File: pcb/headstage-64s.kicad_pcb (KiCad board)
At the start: 6 copper layers, 19 x 19 mm, 119 parts, among them J1 Conn_Coaxial, J2 DF40C-70DP-0.4V(51), J5 PINHD-1x7_ONIXJTAG-RevA, SW1 R-668049, U1 RHD2164, U10 NCP163AFCT120T2G, U11 W25Q80EWUXIE, U12 DSC6011JI1A-050.0000, U13 NCP163AFCT330T2G, U2 TS4231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

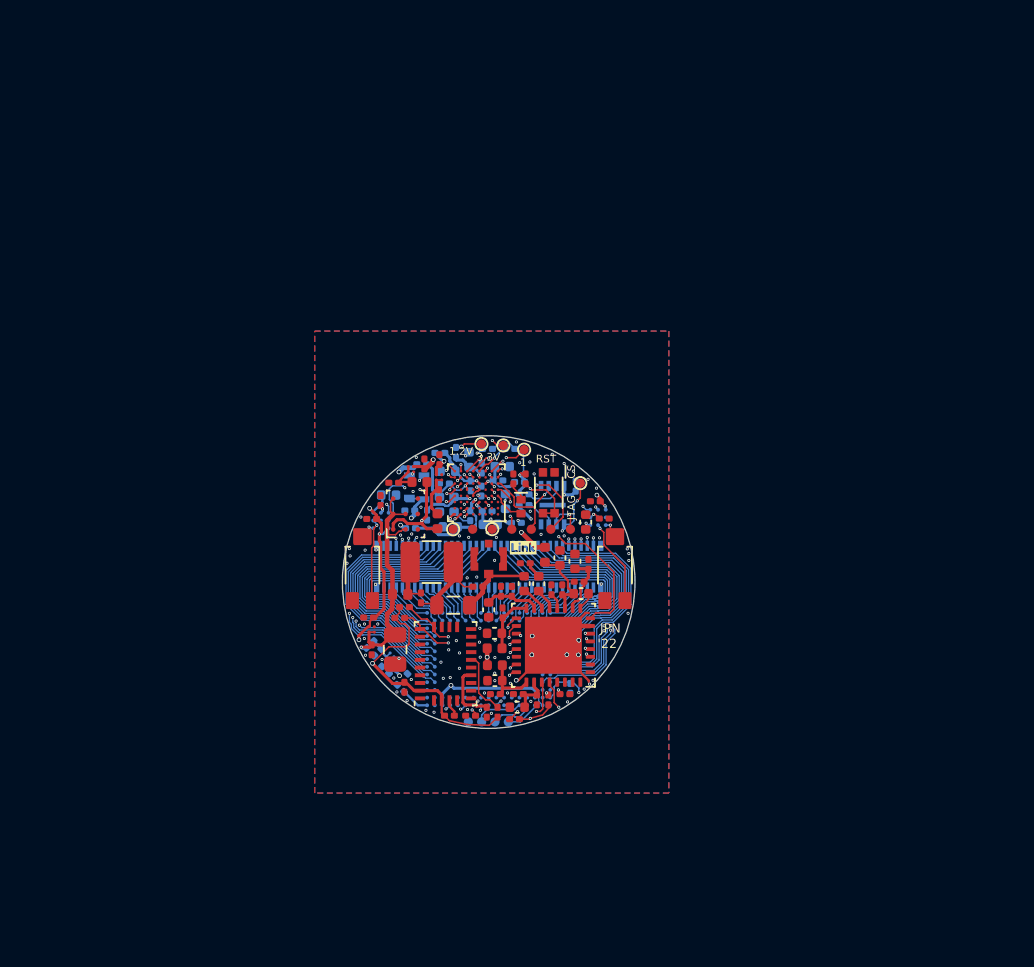
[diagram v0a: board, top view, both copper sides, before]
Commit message: Rev. A initial design prior to fab comments
- BOM simplification
- Added my initials to the board
- Made the board more easy to panlize
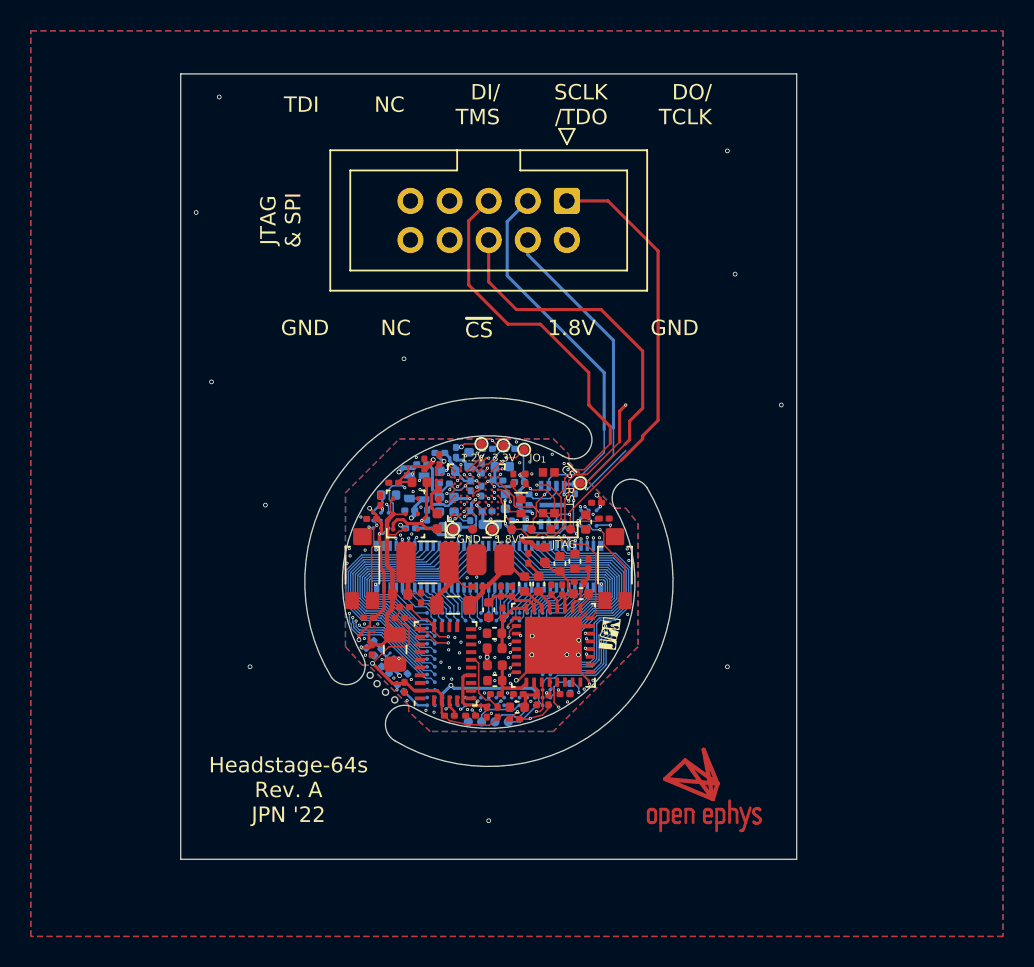
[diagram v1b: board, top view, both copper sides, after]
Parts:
- removed kibuzzard-61E6E0C5: G***, kibuzzard-61E6E0C5
- added ?: , jonnew-eagle:OE-LOGO-7X5, F.Cu at (137.2, 77.3)
- added G***: LOGO, LOGO, F.Cu at (131.3, 66.3)
- added J3: SBH11-PBPC-D05-ST-BK, Connector_IDC:IDC-Header_2x05_P2.54mm_Vertical, F.Cu at (128.6, 38.2)
- added JP1: Jumper_2_Open, jonnew:OE_SolderJumper-2_0201_Open_Pad, B.Cu at (125.9, 59.2)
- C51, C52: value 1.0uF -> 1uF
- D2: value LED -> SML-P11UTT86R
- J1: value Conn_Coaxial -> CONMHF4-SMD-G-T; footprint jonnew:LINX_CONMHF4-SMD-G -> Headstage-64s:Coax-Adapter
- R3: value ? -> 39.2,1%
- R4: value ? -> 78.7k,1%
- R6: value ? -> 40.2k,1%
- U5: value TPS8269xxxSIPR -> TPS82695
- moved U6 0.60 mm to (130.0, 58.9)
- moved REF** 0.44 mm to (126.6, 55.2)
- moved R15 0.38 mm to (126.1, 61.5), turned to 90 degrees
- moved C35 0.38 mm to (128.1, 61.8)
- moved L12 0.36 mm to (125.0, 59.4), turned to 90 degrees
- moved L3 0.27 mm to (119.5, 61.7)
- moved C42 0.18 mm to (129.1, 57.0), turned to -90 degrees
- moved C26 0.12 mm to (130.5, 57.9)
- moved J1 0.12 mm to (123.6, 61.5)
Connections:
- U11 pad 1: /FPGA/~{CS}_{Flash} -> Net-(JP1-Pad1)
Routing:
- net /FPGA/TDI: track 3.01 -> 42.6 mm, vias 2 -> 3
- net /FPGA/DO_{Flash}/TCK: track 7.82 -> 34.5 mm
- net /FPGA/DI_{Flash}/TMS: track 7.74 -> 34.1 mm
- net /FPGA/~{CS}_{Flash}: track 9.74 -> 35.7 mm, vias 3 -> 4
- net /FPGA/SCLK_{Flash}/TDO: track 6.64 -> 30.9 mm
- net +1V8: track 49.6 -> 68.5 mm
- net GND: track 14.2 -> 17.6 mm, vias 89 -> 101
- net Net-(JP1-Pad1): track 0.00 -> 3.02 mm
- net /FPGA/PDB_{Ser}: track 19.4 -> 17.7 mm
- net /DC Tap & Regulation/RF+DC: track 4.98 -> 6.04 mm
- net Net-(R17-Pad2): track 0.78 -> 1.72 mm
- net /3D Pose/PD_{1}-: track 1.17 -> 1.79 mm
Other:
- board size 19 x 19 mm -> 40 x 51 mm
- board text added: "1.8V"
- board text added: "DI/ TMS"
- board text added: "DO/ TCLK"
- board text added: "Headstage-64s Rev. A JPN '22"
- board text added: "IO_{1}"
- board text added: "JTAG & SPI"
- board text added: "NC"
- board text added: "SCLK /TDO"
- board text added: "TDI"
- board text removed: "'22"
- board text removed: "1"
- board text removed: "JPN"

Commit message: Small changes before speedy fabrication
- This is revision A
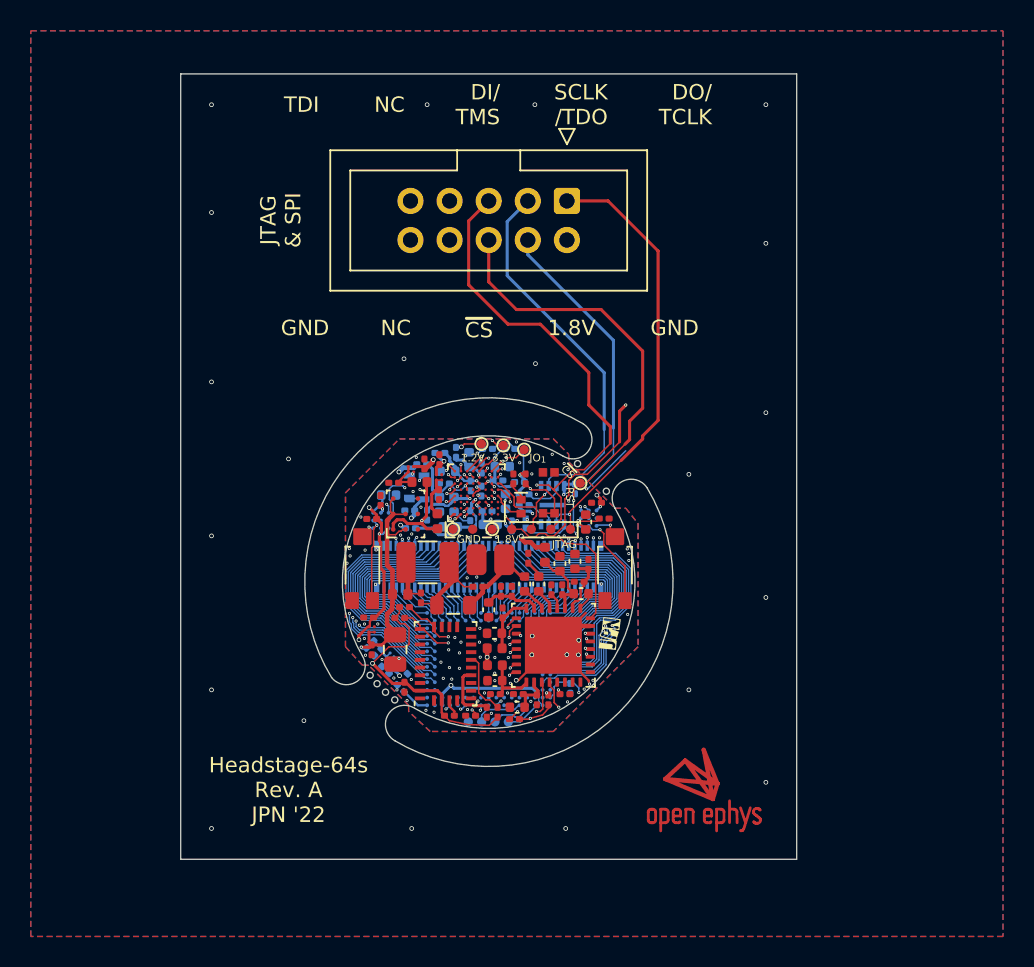
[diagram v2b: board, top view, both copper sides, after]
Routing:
- net GND: vias 101 -> 111
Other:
- outline, holes or cut-outs redrawn

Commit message: Start of revision B
- Address the following issues
1. The photodiode anode is on pin 3, not pin 2
2. No paste on coax connector
3. CRESET_B needs to come out to programming header
4. Need PU on CS line.
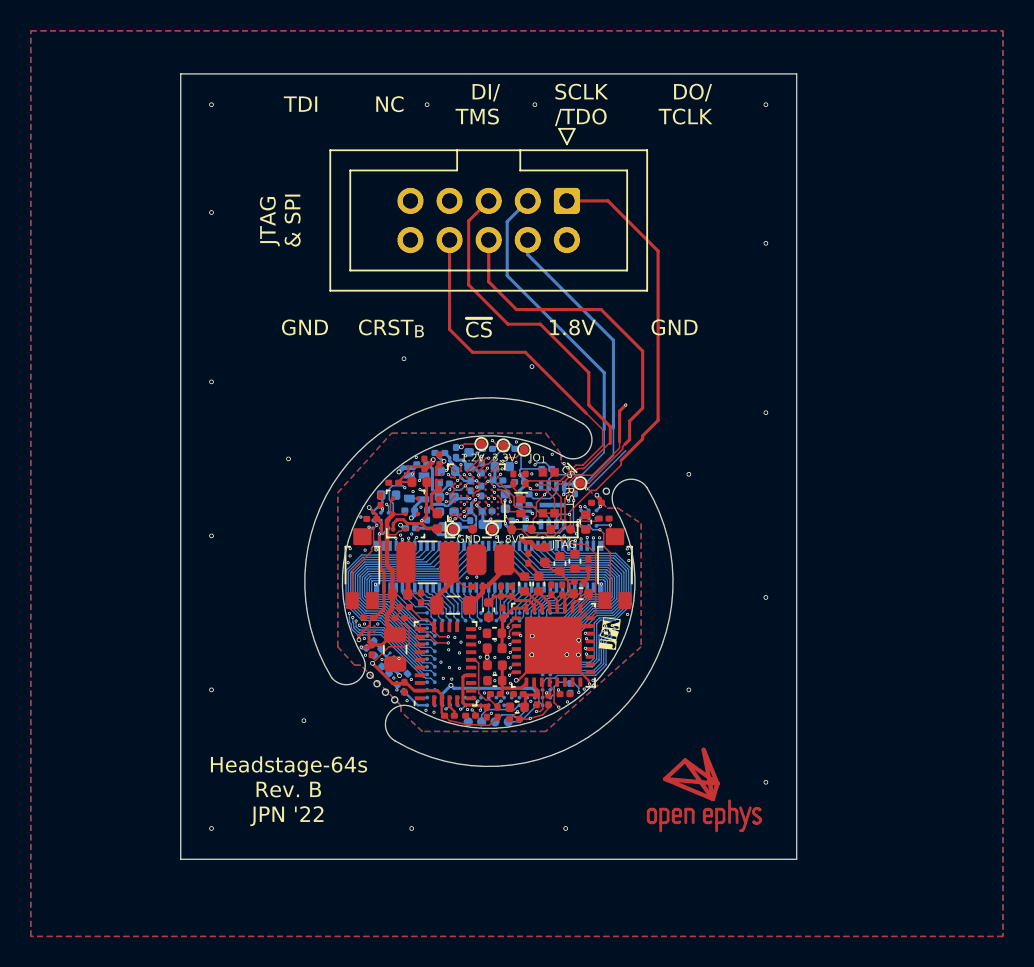
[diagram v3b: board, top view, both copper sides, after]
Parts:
- removed REF**: OE_LOGO-NOTXT-MASK-3.5x2.5, jonnew:OE_LOGO-NOTXT-MASK-3.5x2.5
- added G***: LOGO, LOGO, B.Cu at (126.5, 54.7)
- added R14: 4.7k, Resistor_SMD:R_0201_0603Metric, B.Cu at (127.3, 55.6)
- R1, R2: value 1.2k -> 1k
- U5: value TPS82695 -> TPS826951
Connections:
- D1 pad 2: /3D Pose/PD_{0}+ -> unconnected-(D1-Pad2)
- D1 pad 3: (no net) -> /3D Pose/PD_{0}+
- D3 pad 2: /3D Pose/PD_{1}+ -> unconnected-(D3-Pad2)
- D3 pad 3: (no net) -> /3D Pose/PD_{1}+
- J3 pad 8: unconnected-(J3-Pad8) -> /FPGA/CRESET_{B}
- R20 pad 2: Net-(R20-Pad2) -> /FPGA/CRESET_{B}
- SW1 pad 1: Net-(R20-Pad2) -> /FPGA/CRESET_{B}
- U8 pad E2: Net-(R20-Pad2) -> /FPGA/CRESET_{B}
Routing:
- net /FPGA/CRESET_{B}: track 0.00 -> 32.1 mm, vias 0 -> 2
- net Net-(R20-Pad2): track 6.65 -> 0.00 mm, vias 2 -> 0
- net /FPGA/~{CS}_{Flash}: track 35.7 -> 40.6 mm, vias 4 -> 5
- net +1V8: track 68.5 -> 69.7 mm
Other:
- outline, holes or cut-outs redrawn
- board text added: "1"
- board text added: "2"
- board text added: "3"
- board text added: "Aux"
- board text added: "CRST_{B}"
- board text added: "G"
- board text added: "HS-64s Rev.B '22"
- board text added: "Headstage-64s Rev. B JPN '22"
- board text removed: "Aux0"
- board text removed: "Aux1"
- board text removed: "Aux2"
- board text removed: "HS-64s Rev.A '22"
- board text removed: "Headstage-64s Rev. A JPN '22"
- board text removed: "Ref"
